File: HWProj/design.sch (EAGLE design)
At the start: 15 parts, among them IC1 LM311N, IC2 TL071P, IC3 TL071P, IC4 TL071P, IC5 LM311N, Q1 2N3904, Q2 2N3904

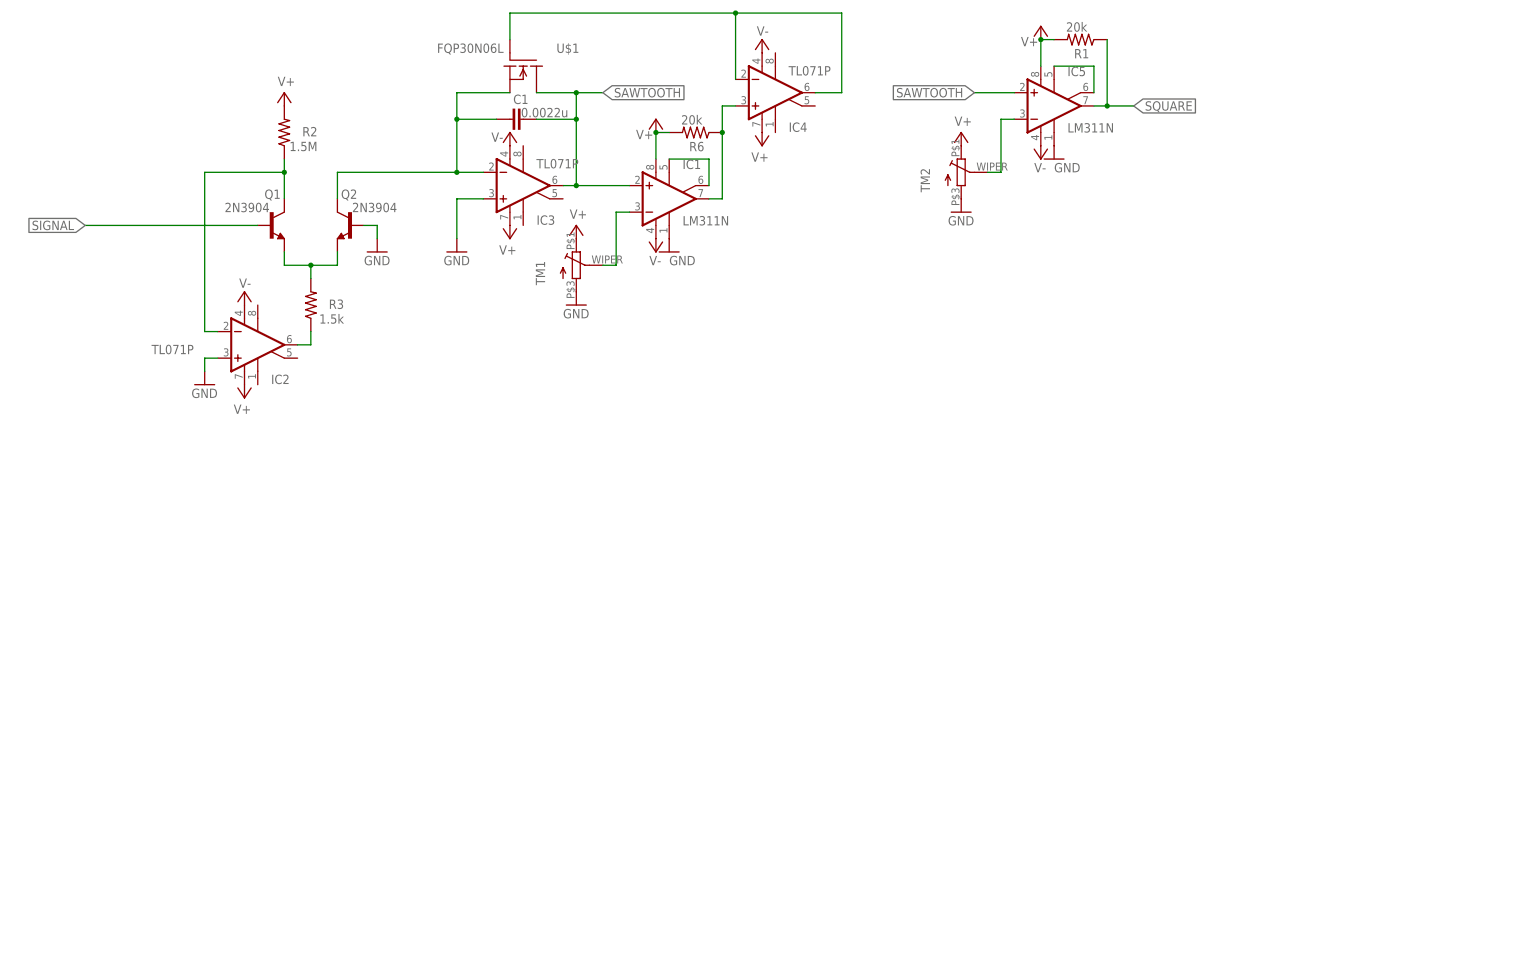
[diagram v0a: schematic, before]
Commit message: 1st order vcf and 2nd order manual filter added (unsimulated)
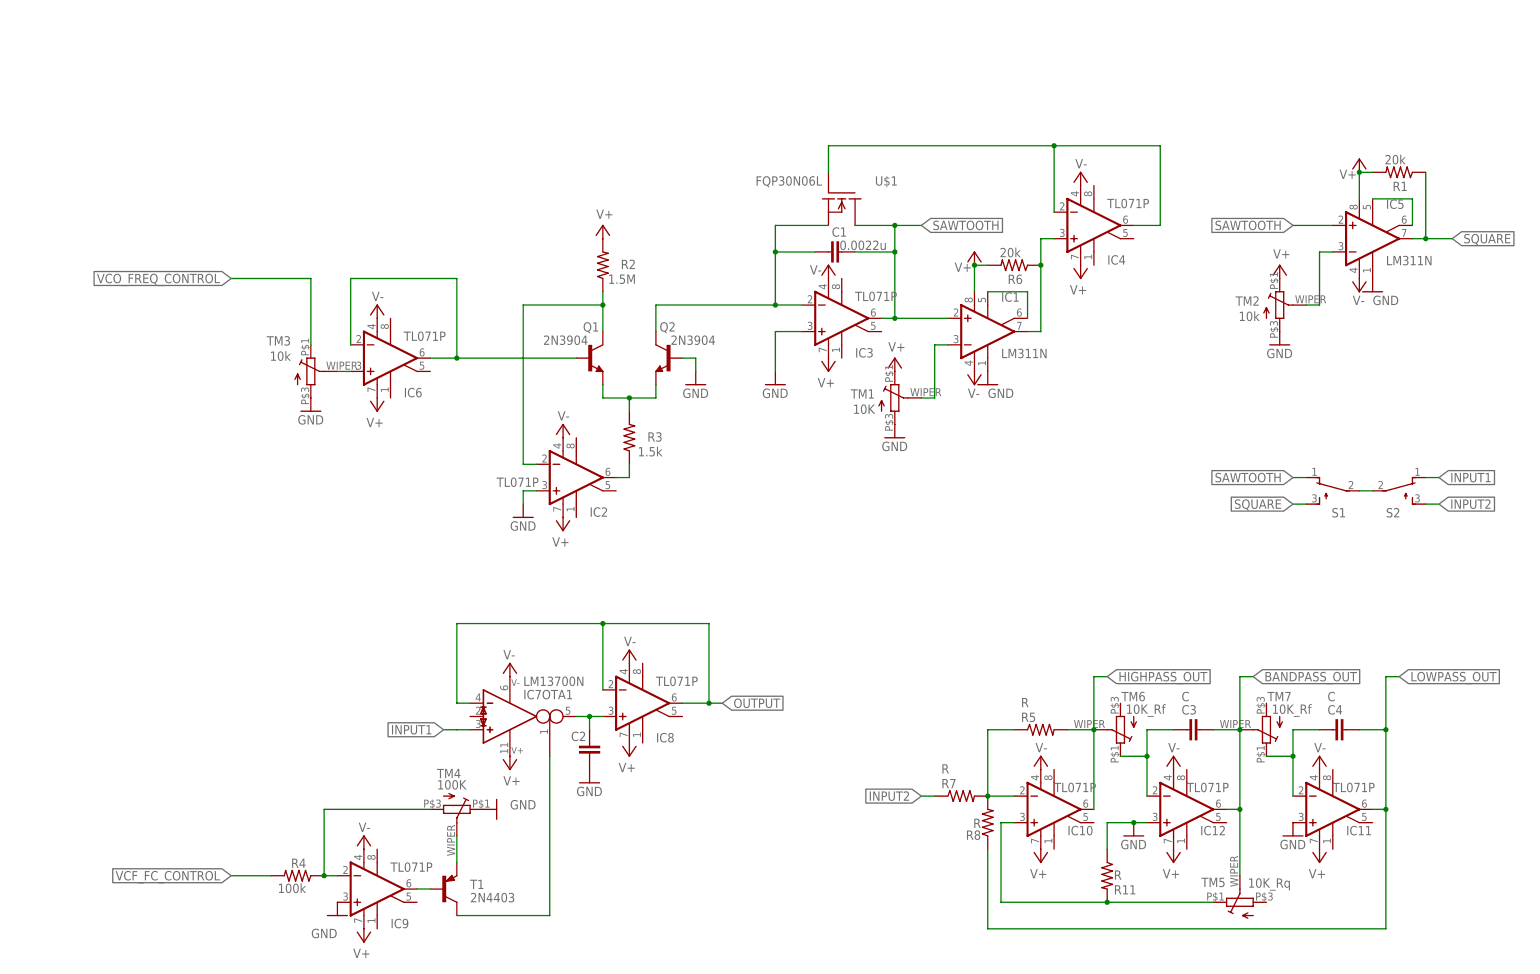
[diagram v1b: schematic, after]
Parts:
- added C2: 0.0022u, HyTechDevices:CAPCAP_WIMA
- added C3, C4: C, HyTechDevices:CAPCAP_WIMA
- added IC10, IC11, IC12, IC6, IC8, IC9: TL071P, linear:TL071P
- added IC7: LM13700N, ota:LM13700N
- added R11, R5, R7, R8: R, HyTechDevices:RESISTORAXIAL-0.3
- added R4: 100k, HyTechDevices:RESISTORAXIAL-0.3
- added S1, S2: TL32PO, switch:TL32PO
- added T1: 2N4403, transistor-neu-to92:2N4403-PNP-TO92-EBC
- added TM3: 10k, HyTechDevices:TRIMPOT
- added TM4: 100K, HyTechDevices:TRIMPOT
- added TM5: 10K_Rq, HyTechDevices:TRIMPOT
- added TM6, TM7: 10K_Rf, HyTechDevices:TRIMPOT
- TM1: value (none) -> 10K
- TM2: value (none) -> 10k
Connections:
- removed net SIGNAL: Q1.B
- new net BANDPASS_OUT: C3.1, IC12.OUT, TM5.S, TM7.S
- new net HIGHPASS_OUT: IC10.OUT, R5.2, TM6.S
- new net INPUT1: IC7OTA1.IN_P, S2.O
- new net INPUT2: R7.1, S2.S
- new net LOWPASS_OUT: C4.1, IC11.OUT, R8.1
- new net N$13: T1.E, TM4.S
- new net N$14: IC6.-IN, IC6.OUT, Q1.B
- new net N$15: IC9.-IN, R4.1, TM4.A
- new net N$16: IC9.OUT, T1.B
- new net N$17: IC7OTA1.I_BIAS, T1.C
- new net N$18: IC10.-IN, R5.1, R7.2, R8.2
- new net N$19: S1.P, S2.P
- new net N$20: C3.2, IC12.-IN, TM6.E
- new net N$22: C4.2, IC11.-IN, TM7.E
- new net N$25: IC10.+IN, R11.2, TM5.E
- new net N$3: C2.2, IC7OTA1.OUT, IC8.+IN
- new net N$4: IC6.+IN, TM3.S
- new net OUTPUT: IC7OTA1.IN_N, IC8.-IN, IC8.OUT
- new net VCF_FC_CONTROL: R4.2
- new net VCO_FREQ_CONTROL: TM3.E
- net GND: now also C2.1, IC11.+IN, IC12.+IN, IC9.+IN, R11.1, TM3.A, TM4.E
- net SAWTOOTH: now also S1.O
- net SQUARE: now also S1.S
- net V+: now also IC10.V+, IC11.V+, IC12.V+, IC6.V+, IC7SUPPLY.V+, IC8.V+, IC9.V+
- net V-: now also IC10.V-, IC11.V-, IC12.V-, IC6.V-, IC7SUPPLY.V-, IC8.V-, IC9.V-
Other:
- note added: "1st order VCF"
- note added: "Q, omega independently variable two-pole filter circuit"
- note added: "experiment and determine set values for resistor divider here"
- note added: "input sanitization"
- note added: "pots Rf to be replaced by OTAs with i_con source for Fs voltage control"
- note added: "signal routing"
- note removed: "0-100mV range"
- moved on the sheet: C1, IC1, IC2, IC3, IC4, IC5, Q1, Q2, R1, R2, R3, R6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

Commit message: tested two-pole filter circuit, determined r/c val
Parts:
- C3, C4: value C -> 0.0022uF
- R11, R5, R7, R8: value R -> 1k
- TM5: value 10K_Rq -> 50k_Rq
- TM6: value 10K_Rf -> 50k_Rf
- TM7: value 10K_Rf -> 50K_Rf
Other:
- note added: "Fs = 1 / (2*pi*Rf*C)"
- note added: "Q = (Rq+R) / R"
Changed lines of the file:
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@@
 <?xml version="1.0" encoding="utf-8"?>
 <!DOCTYPE eagle SYSTEM "eagle.dtd">
-<eagle version="9.1.0">
+<eagle version="9.5.2">
 <drawing>
 <settings>
@@
 <part name="SUPPLY23" library="supply2" library_urn="urn:adsk.eagle:library:372" deviceset="V-" device=""/>
 <part name="IC10" library="linear" library_urn="urn:adsk.eagle:library:262" deviceset="TL071" device="P" package3d_urn="urn:adsk.eagle:package:16409/2"/>
-<part name="R5" library="HyTechDevices" deviceset="RESISTOR" device="AXIAL-0.3" value="R"/>
-<part name="R7" library="HyTechDevices" deviceset="RESISTOR" device="AXIAL-0.3" value="R"/>
-<part name="R8" library="HyTechDevices" deviceset="RESISTOR" device="AXIAL-0.3" value="R"/>
-<part name="C3" library="HyTechDevices" deviceset="CAP" device="CAP_WIMA" value="C"/>
-<part name="C4" library="HyTechDevices" deviceset="CAP" device="CAP_WIMA" value="C"/>
+<part name="R5" library="HyTechDevices" deviceset="RESISTOR" device="AXIAL-0.3" value="1k"/>
+<part name="R7" library="HyTechDevices" deviceset="RESISTOR" device="AXIAL-0.3" value="1k"/>
+<part name="R8" library="HyTechDevices" deviceset="RESISTOR" device="AXIAL-0.3" value="1k"/>
+<part name="C3" library="HyTechDevices" deviceset="CAP" device="CAP_WIMA" value="0.0022uF"/>
+<part name="C4" library="HyTechDevices" deviceset="CAP" device="CAP_WIMA" value="0.0022uF"/>
 <part name="SUPPLY24" library="supply2" library_urn="urn:adsk.eagle:library:372" deviceset="V+" device=""/>
 <part name="SUPPLY25" library="supply2" library_urn="urn:adsk.eagle:library:372" deviceset="V-" device=""/>
@@
 <part name="GND12" library="HyTechSymbols" deviceset="GND" device=""/>
 <part name="GND13" library="HyTechSymbols" deviceset="GND" device=""/>
-<part name="R11" library="HyTechDevices" deviceset="RESISTOR" device="AXIAL-0.3" value="R"/>
-<part name="TM5" library="HyTechDevices" deviceset="TRIMPOT" device="" value="10K_Rq"/>
-<part name="TM6" library="HyTechDevices" deviceset="TRIMPOT" device="" value="10K_Rf"/>
-<part name="TM7" library="HyTechDevices" deviceset="TRIMPOT" device="" value="10K_Rf"/>
+<part name="R11" library="HyTechDevices" deviceset="RESISTOR" device="AXIAL-0.3" value="1k"/>
+<part name="TM5" library="HyTechDevices" deviceset="TRIMPOT" device="" value="50k_Rq"/>
+<part name="TM6" library="HyTechDevices" deviceset="TRIMPOT" device="" value="50k_Rf"/>
+<part name="TM7" library="HyTechDevices" deviceset="TRIMPOT" device="" value="50K_Rf"/>
 <part name="S2" library="switch" library_urn="urn:adsk.eagle:library:380" deviceset="TL32PO" device="" package3d_urn="urn:adsk.eagle:package:27745/1"/>
 </parts>
@@
 <text x="228.6" y="35.56" size="1.778" layer="150">signal routing</text>
 <text x="167.64" y="-73.66" size="1.778" layer="150">pots Rf to be replaced by OTAs with i_con source for Fs voltage control</text>
+<text x="246.38" y="-48.26" size="1.778" layer="150">Q = (Rq+R) / R</text>
+<text x="246.38" y="-40.64" size="1.778" layer="150">Fs = 1 / (2*pi*Rf*C)</text>
 </plain>
 <instances>
@@
 <attribute name="VALUE" x="53.34" y="48.26" size="1.778" layer="96" rot="MR180"/>
 </instance>
-<instance part="IC7" gate="OTA1" x="73.66" y="-25.4" rot="MR180"/>
-<instance part="IC7" gate="SUPPLY" x="73.66" y="-25.4" rot="MR180"/>
+<instance part="IC7" gate="OTA1" x="73.66" y="-25.4" smashed="yes" rot="MR180">
+<attribute name="NAME" x="76.2" y="-20.32" size="1.778" layer="95" rot="MR180"/>
+<attribute name="VALUE" x="76.2" y="-17.78" size="1.778" layer="96" rot="MR180"/>
+</instance>
+<instance part="IC7" gate="SUPPLY" x="73.66" y="-25.4" smashed="yes" rot="MR180"/>
 <instance part="SUPPLY16" gate="1" x="73.66" y="-15.24" smashed="yes" rot="MR180">
 <attribute name="VALUE" x="72.39" y="-12.7" size="1.778" layer="96" rot="MR180"/>
@@
 <wire x1="185.42" y1="-43.18" x2="185.42" y2="-27.94" width="0.1524" layer="91"/>
 <wire x1="185.42" y1="-27.94" x2="180.34" y2="-27.94" width="0.1524" layer="91"/>
-<wire x1="185.42" y1="-27.94" x2="185.42" y2="-17.78" width="0.1524" layer="91"/>
-<wire x1="185.42" y1="-17.78" x2="187.96" y2="-17.78" width="0.1524" layer="91"/>
 <junction x="185.42" y="-27.94"/>
-<label x="187.96" y="-17.78" size="1.778" layer="95" xref="yes"/>
 <pinref part="TM6" gate="G$1" pin="S"/>
 </segment>
@@
 <wire x1="213.36" y1="-43.18" x2="210.82" y2="-43.18" width="0.1524" layer="91"/>
 <junction x="213.36" y="-43.18"/>
-<wire x1="213.36" y1="-27.94" x2="213.36" y2="-17.78" width="0.1524" layer="91"/>
 <junction x="213.36" y="-27.94"/>
-<wire x1="213.36" y1="-17.78" x2="215.9" y2="-17.78" width="0.1524" layer="91"/>
-<label x="215.9" y="-17.78" size="1.778" layer="95" xref="yes"/>
 <pinref part="TM5" gate="G$1" pin="S"/>
 <wire x1="213.36" y1="-55.88" x2="213.36" y2="-43.18" width="0.1524" layer="91"/>

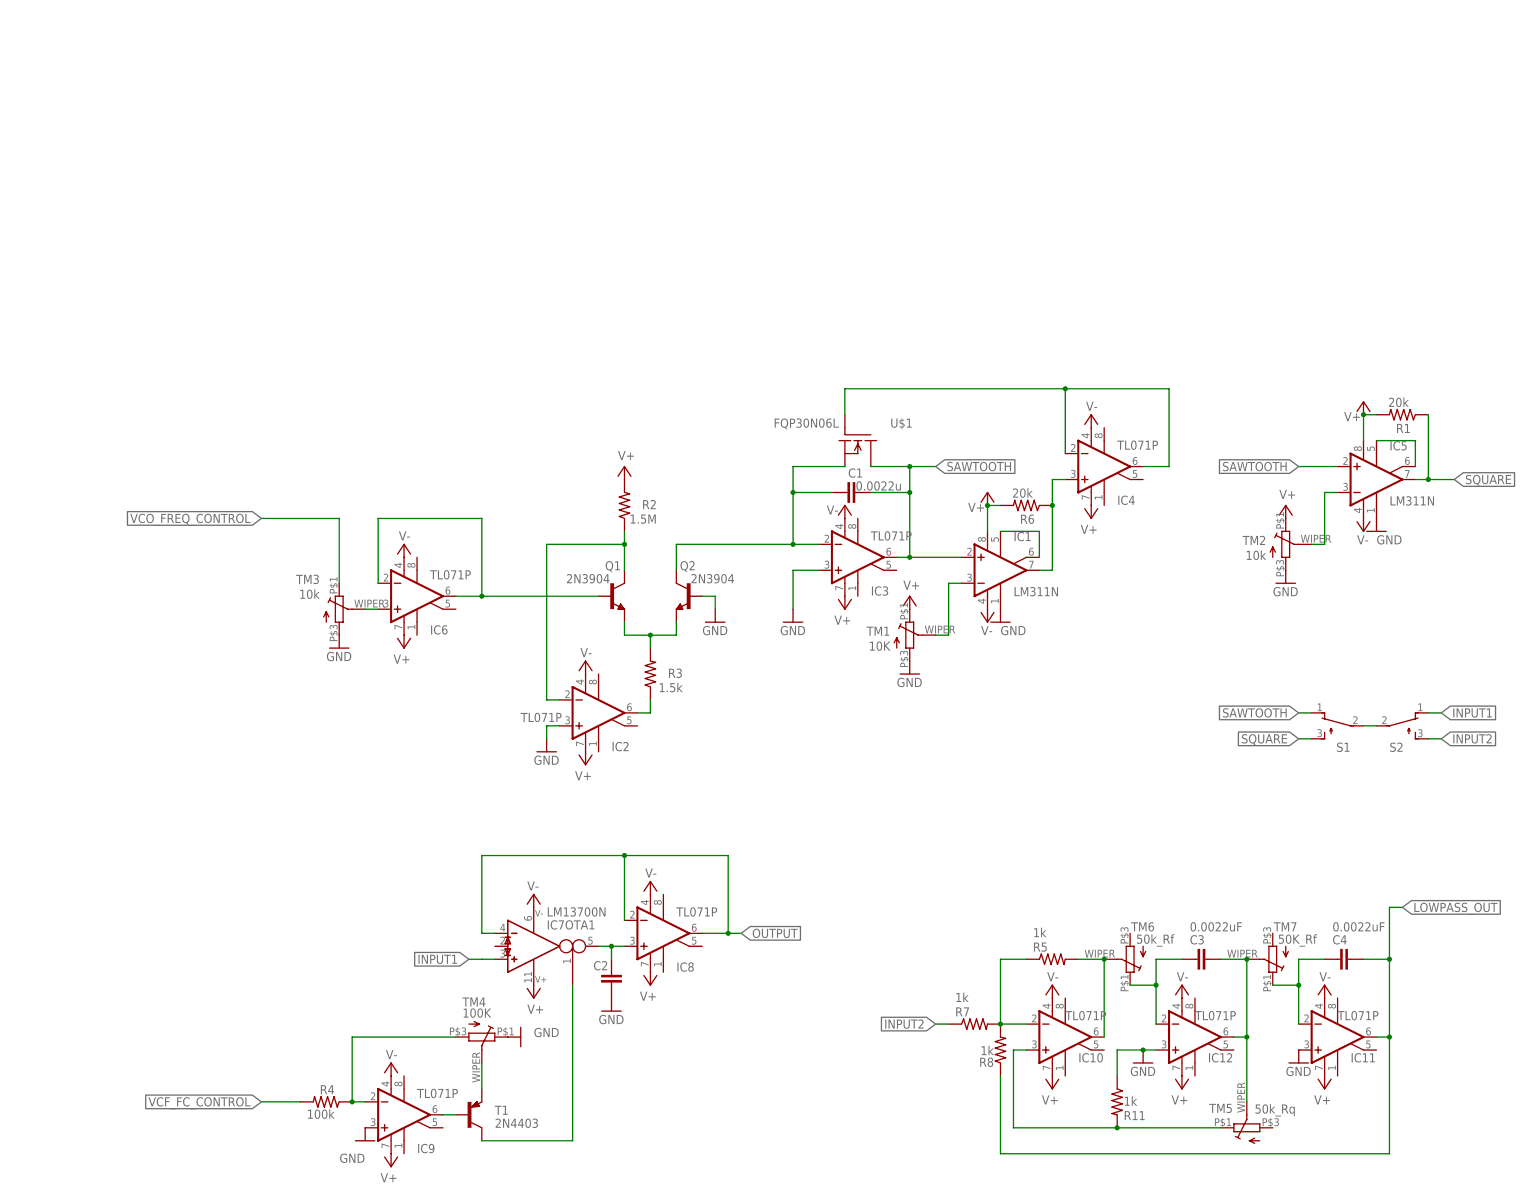
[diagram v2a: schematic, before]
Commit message: removed extraneous components for analog--complete
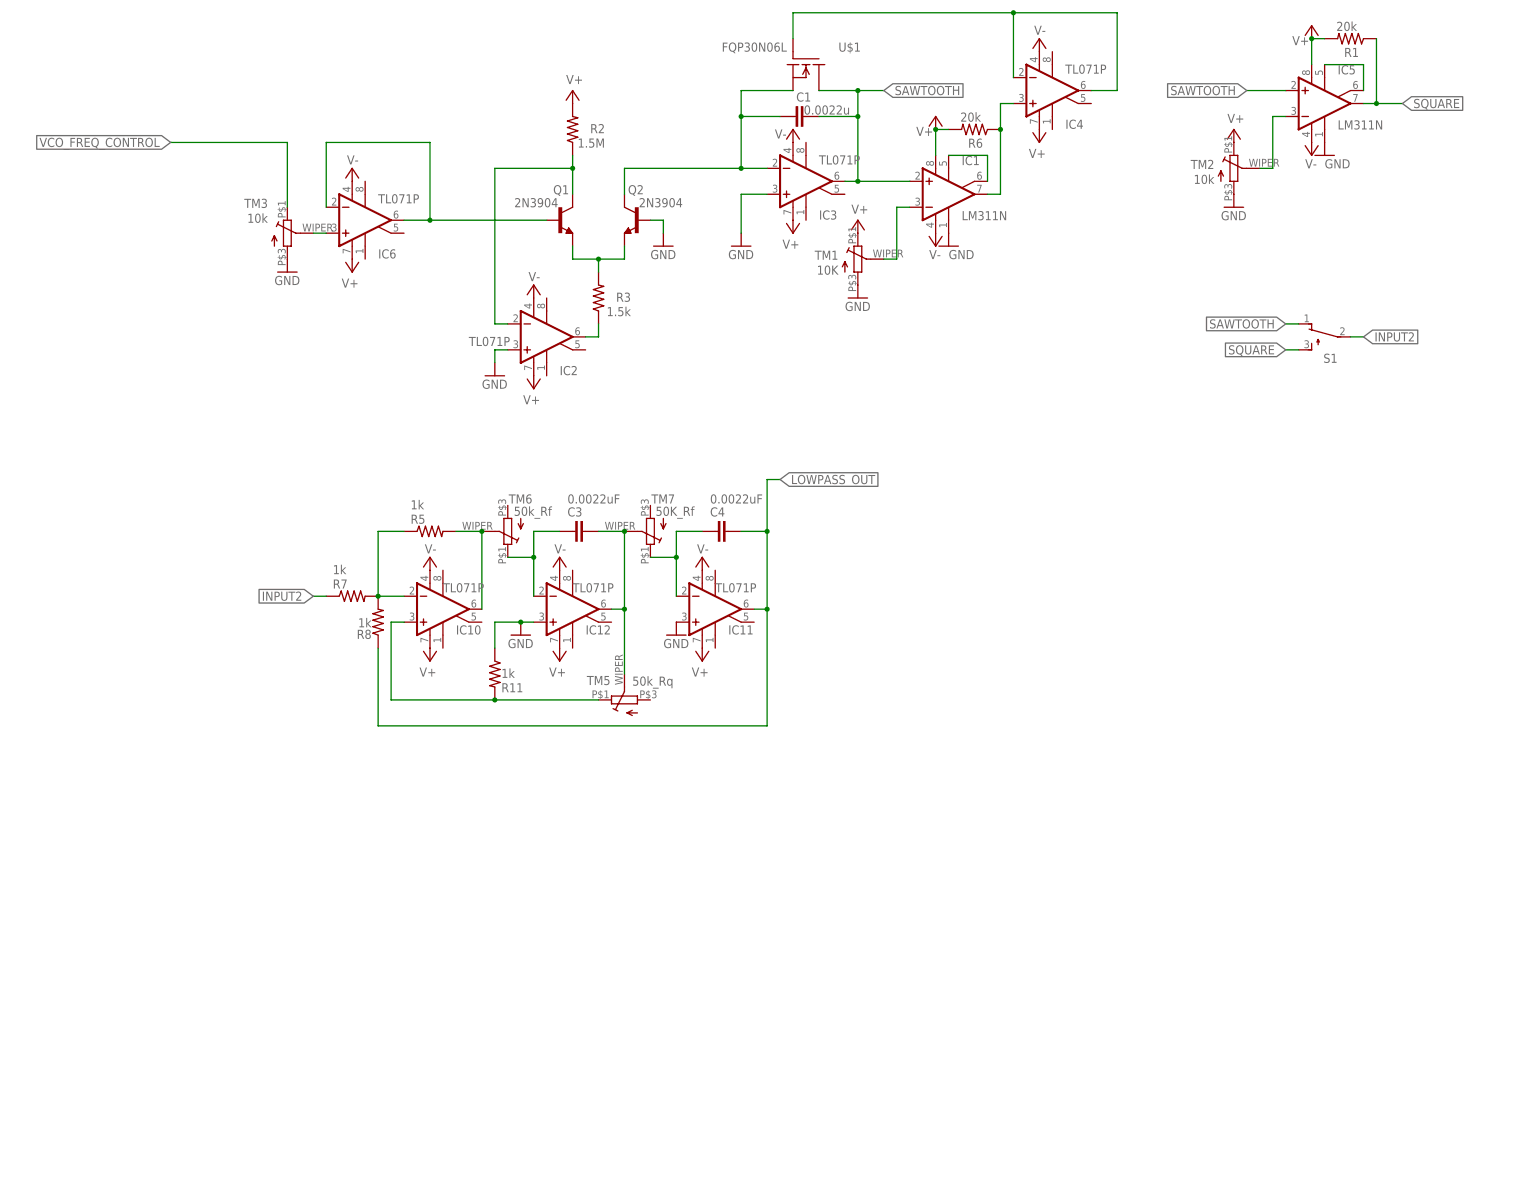
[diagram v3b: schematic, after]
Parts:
- removed C2: 0.0022u, HyTechDevices:CAPCAP_WIMA
- removed IC7: LM13700N, ota:LM13700N
- removed IC8, IC9: TL071P, linear:TL071P
- removed R4: 100k, HyTechDevices:RESISTORAXIAL-0.3
- removed S2: TL32PO, switch:TL32PO
- removed T1: 2N4403, transistor-neu-to92:2N4403-PNP-TO92-EBC
- removed TM4: 100K, HyTechDevices:TRIMPOT
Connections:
- removed net INPUT1: IC7OTA1.IN_P, S2.O
- removed net N$13: T1.E, TM4.S
- removed net N$15: IC9.-IN, R4.1, TM4.A
- removed net N$16: IC9.OUT, T1.B
- removed net N$17: IC7OTA1.I_BIAS, T1.C
- removed net N$19: S1.P, S2.P
- removed net N$3: C2.2, IC7OTA1.OUT, IC8.+IN
- removed net OUTPUT: IC7OTA1.IN_N, IC8.-IN, IC8.OUT
- removed net VCF_FC_CONTROL: R4.2
- net GND: no longer C2.1, IC9.+IN, TM4.E
- net INPUT2: now also S1.P; no longer S2.S
- net V+: no longer IC7SUPPLY.V+, IC8.V+, IC9.V+
- net V-: no longer IC7SUPPLY.V-, IC8.V-, IC9.V-
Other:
- note added: "analog"
- note added: "change the two individual Rf pots to a single dual pot!"
- note added: "solution to create +/- 15V required"
- note removed: "1st order VCF"
- note removed: "experiment and determine set values for resistor divider here"
- note removed: "pots Rf to be replaced by OTAs with i_con source for Fs voltage control"
- moved on the sheet: C1, C3, C4, IC1, IC10, IC11, IC12, IC2, IC3, IC4, IC5, IC6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
